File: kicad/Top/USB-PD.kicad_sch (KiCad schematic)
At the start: 37 parts, among them U3 MCP1804 SOT-23-5

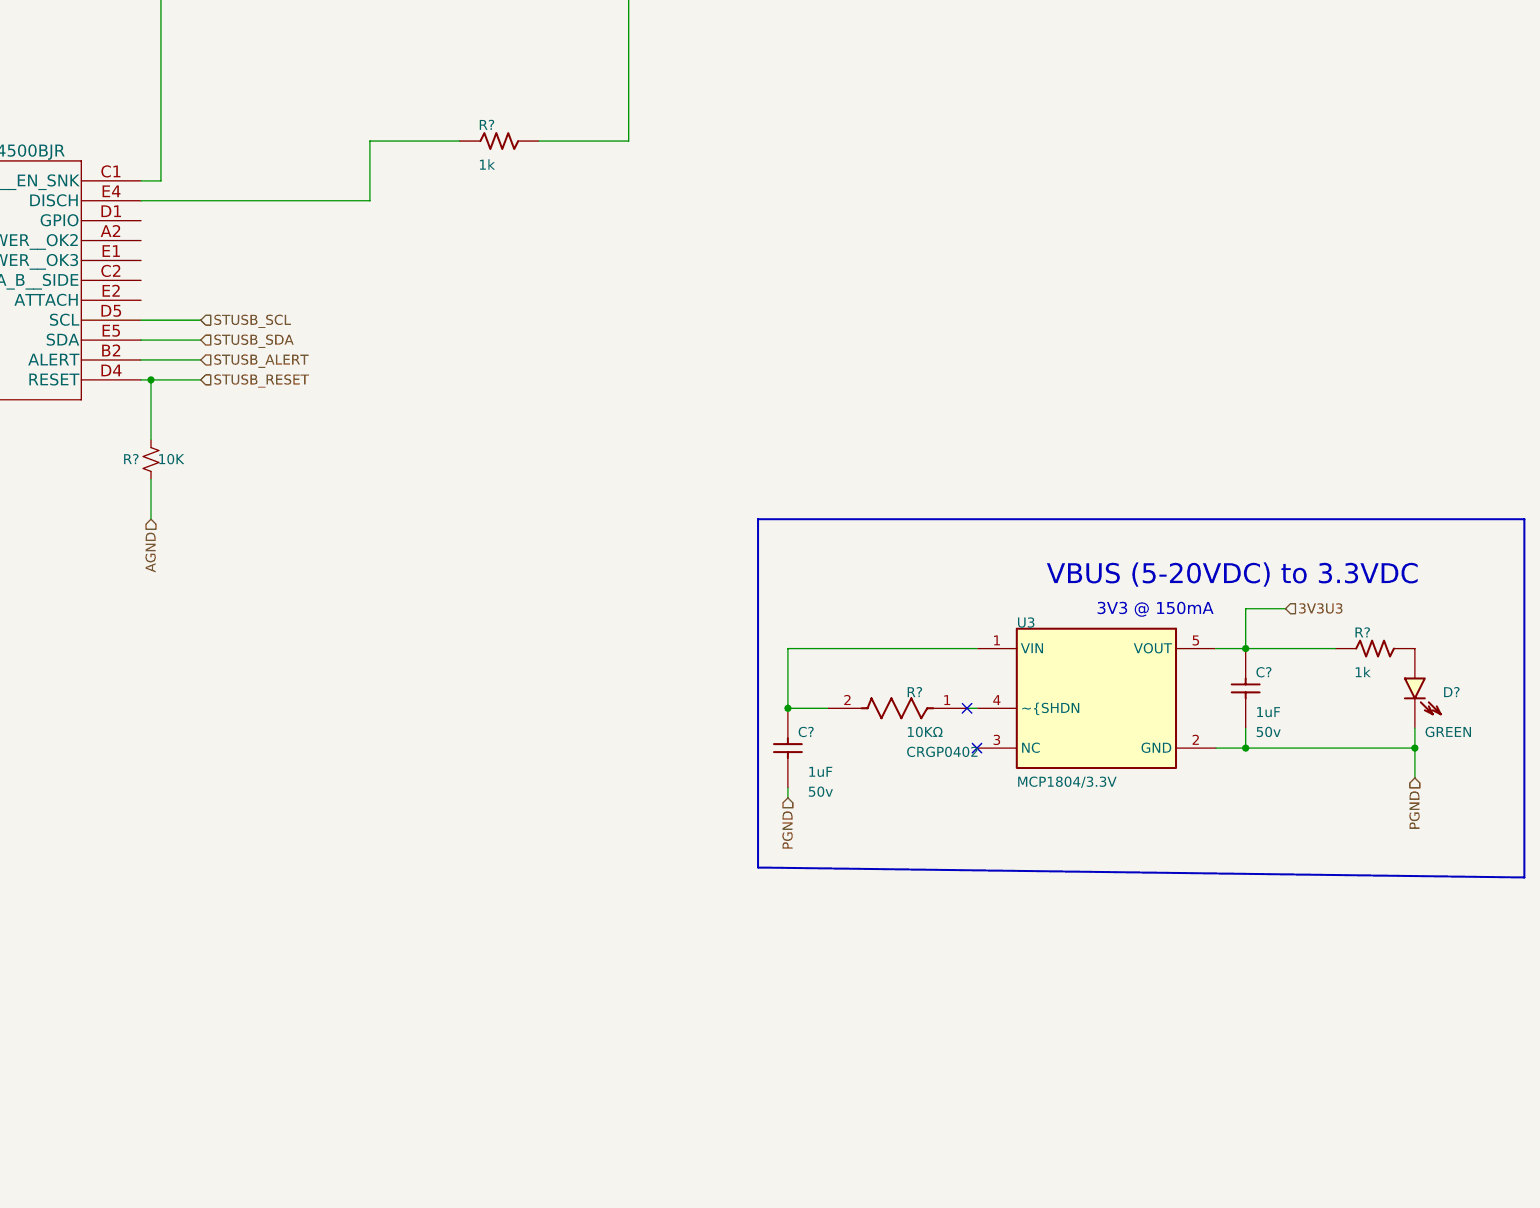
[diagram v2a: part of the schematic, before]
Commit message: Added 3 leds for Pok2,3 and attach
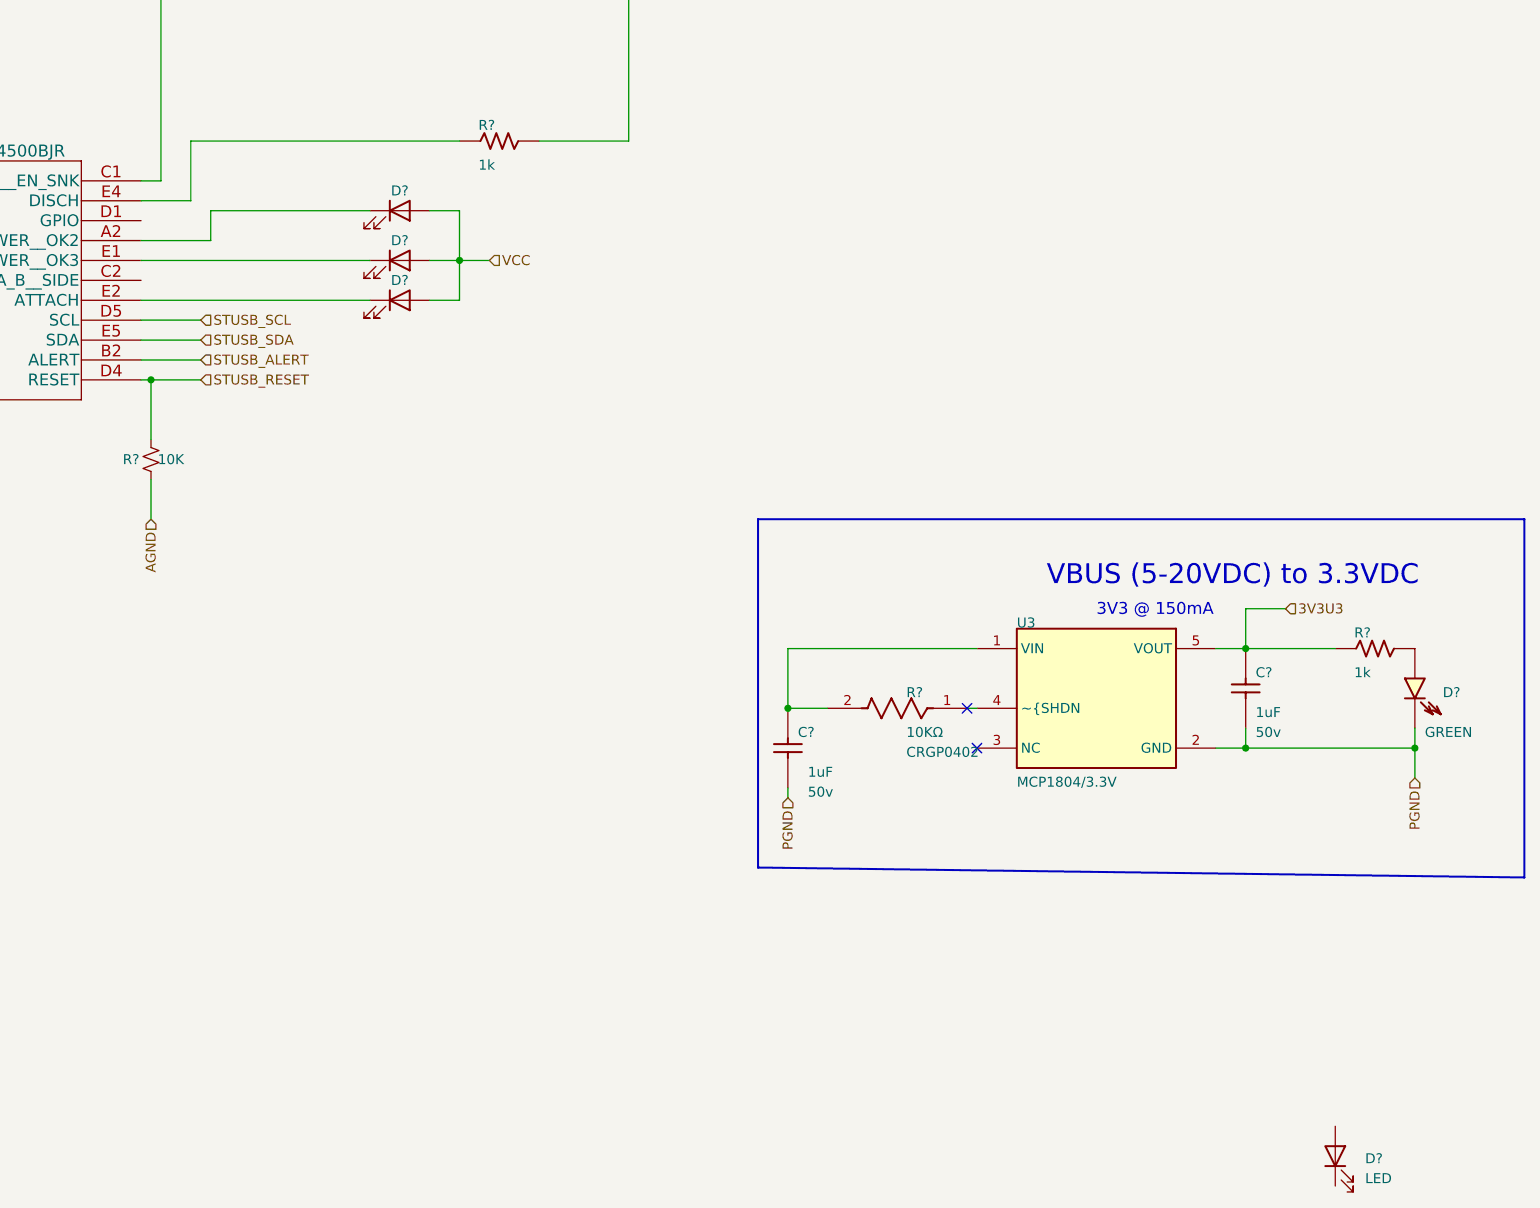
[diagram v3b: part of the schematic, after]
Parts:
- added D? (x4): LED, symbol Device:LED
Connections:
- net VCC: now also D?.2 (A), D?.2 (A), D?.2 (A)
- net at U?.A2 (POWER__OK2): now also D?.1 (K)
- net at U?.E1 (POWER__OK3): now also D?.1 (K)
- net at U?.E2 (ATTACH): now also D?.1 (K)
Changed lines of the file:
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@@
   (junction (at 443.23 454.66) (diameter 0) (color 0 0 0 0)
+  )
+  (junction (at 603.25 411.48) (diameter 0) (color 0 0 0 0)
   )
   (junction (at 444.5 414.02) (diameter 0) (color 0 0 0 0)
@@
     (stroke (width 0) (type default) (color 0 0 0 0))
   )
+  (wire (pts (xy 562.61 403.86) (xy 568.96 403.86))
+    (stroke (width 0) (type default) (color 0 0 0 0))
+  )
   (wire (pts (xy 614.68 300.99) (xy 614.68 306.07))
     (stroke (width 0) (type default) (color 0 0 0 0))
@@
   (wire (pts (xy 417.83 361.95) (xy 416.56 361.95))
     (stroke (width 0.254) (type default) (color 0 0 0 0))
+  )
+  (wire (pts (xy 562.61 416.56) (xy 591.82 416.56))
+    (stroke (width 0) (type default) (color 0 0 0 0))
   )
   (wire (pts (xy 480.06 300.99) (xy 560.07 300.99))
@@
     (stroke (width 0.254) (type default) (color 0 0 0 0))
   )
-  (wire (pts (xy 591.82 403.86) (xy 591.82 396.24))
-    (stroke (width 0) (type default) (color 0 0 0 0))
-  )
   (wire (pts (xy 613.41 396.24) (xy 624.84 396.24))
     (stroke (width 0) (type default) (color 0 0 0 0))
@@
   (wire (pts (xy 577.85 317.5) (xy 598.17 317.5))
     (stroke (width 0.254) (type default) (color 0 0 0 0))
+  )
+  (wire (pts (xy 571.5 408.94) (xy 571.5 405.13))
+    (stroke (width 0) (type default) (color 0 0 0 0))
   )
   (wire (pts (xy 478.79 416.56) (xy 478.79 414.02))
@@
     (stroke (width 0) (type default) (color 0 0 0 0))
   )
+  (wire (pts (xy 562.61 411.48) (xy 591.82 411.48))
+    (stroke (width 0) (type default) (color 0 0 0 0))
+  )
+  (wire (pts (xy 571.5 405.13) (xy 591.82 405.13))
+    (stroke (width 0) (type default) (color 0 0 0 0))
+  )
   (wire (pts (xy 386.08 356.87) (xy 386.08 359.41))
     (stroke (width 0.254) (type default) (color 0 0 0 0))
@@
     (stroke (width 0.254) (type default) (color 0 0 0 0))
   )
+  (wire (pts (xy 603.25 411.48) (xy 607.06 411.48))
+    (stroke (width 0) (type default) (color 0 0 0 0))
+  )
   (wire (pts (xy 521.97 382.27) (xy 521.97 386.08))
     (stroke (width 0) (type default) (color 0 0 0 0))
@@
   )
   (wire (pts (xy 448.31 411.48) (xy 478.79 411.48))
+    (stroke (width 0) (type default) (color 0 0 0 0))
+  )
+  (wire (pts (xy 562.61 408.94) (xy 571.5 408.94))
     (stroke (width 0) (type default) (color 0 0 0 0))
   )
@@
     (stroke (width 0) (type default) (color 0 0 0 0))
   )
+  (wire (pts (xy 603.25 416.56) (xy 603.25 411.48))
+    (stroke (width 0) (type default) (color 0 0 0 0))
+  )
   (wire (pts (xy 598.17 308.61) (xy 598.17 317.5))
     (stroke (width 0.254) (type default) (color 0 0 0 0))
@@
     (stroke (width 0.254) (type default) (color 0 0 0 0))
   )
+  (wire (pts (xy 599.44 411.48) (xy 603.25 411.48))
+    (stroke (width 0) (type default) (color 0 0 0 0))
+  )
   (wire (pts (xy 668.02 468.63) (xy 669.29 468.63))
     (stroke (width 0.254) (type default) (color 0 0 0 0))
@@
   (wire (pts (xy 417.83 359.41) (xy 426.72 359.41))
     (stroke (width 0.254) (type default) (color 0 0 0 0))
+  )
+  (wire (pts (xy 599.44 416.56) (xy 603.25 416.56))
+    (stroke (width 0) (type default) (color 0 0 0 0))
   )
   (wire (pts (xy 645.16 468.63) (xy 645.16 461.01))
@@
     (stroke (width 0.254) (type default) (color 0 0 0 0))
   )
-  (wire (pts (xy 591.82 396.24) (xy 603.25 396.24))
+  (wire (pts (xy 568.96 396.24) (xy 603.25 396.24))
     (stroke (width 0) (type default) (color 0 0 0 0))
   )
@@
   (wire (pts (xy 388.62 364.49) (xy 386.08 364.49))
     (stroke (width 0.254) (type default) (color 0 0 0 0))
+  )
+  (wire (pts (xy 568.96 403.86) (xy 568.96 396.24))
+    (stroke (width 0) (type default) (color 0 0 0 0))
   )
   (wire (pts (xy 603.25 300.99) (xy 614.68 300.99))
@@
     (stroke (width 0.254) (type default) (color 0 0 0 0))
   )
+  (wire (pts (xy 603.25 405.13) (xy 603.25 411.48))
+    (stroke (width 0) (type default) (color 0 0 0 0))
+  )
   (wire (pts (xy 562.61 401.32) (xy 565.15 401.32))
     (stroke (width 0) (type default) (color 0 0 0 0))
@@
     (stroke (width 0.254) (type default) (color 0 0 0 0))
   )
+  (wire (pts (xy 599.44 405.13) (xy 603.25 405.13))
+    (stroke (width 0) (type default) (color 0 0 0 0))
+  )
   (wire (pts (xy 459.74 424.18) (xy 483.87 424.18))
     (stroke (width 0) (type default) (color 0 0 0 0))
@@
   )
   (wire (pts (xy 562.61 419.1) (xy 570.23 419.1))
-    (stroke (width 0) (type default) (color 0 0 0 0))
-  )
-  (wire (pts (xy 562.61 403.86) (xy 591.82 403.86))
     (stroke (width 0) (type default) (color 0 0 0 0))
   )
@@
   )
   (hierarchical_label "STUSB_ALERT" (shape input) (at 570.23 424.18 0)
+    (effects (font (size 1.27 1.27)) (justify left))
+  )
+  (hierarchical_label "VCC" (shape input) (at 607.06 411.48 0)
     (effects (font (size 1.27 1.27)) (justify left))
   )
@@
     (pin "B9")
   )
+  (symbol (lib_id "Device:LED") (at 595.63 416.56 0) (unit 1)
+    (in_bom yes) (on_board yes)
+    (property "Reference" "D?" (id 0) (at 595.63 414.02 0))
+    (property "Value" "LED" (id 1) (at 594.0425 412.75 0)
+      (effects (font (size 1.27 1.27)) hide)
+    )
+    (property "Footprint" "" (id 2) (at 595.63 416.56 0)
+      (effects (font (size 1.27 1.27)) hide)
+    )
+    (property "Datasheet" "~" (id 3) (at 595.63 416.56 0)
+      (effects (font (size 1.27 1.27)) hide)
+    )
+    (pin "1")
+    (pin "2")
+  )
   (symbol (lib_id "Device:C_Small") (at 505.46 379.73 90) (unit 1)
     (in_bom yes) (on_board yes)
@@
     (pin "1")
   )
+  (symbol (lib_id "Device:LED") (at 595.63 411.48 0) (unit 1)
+    (in_bom yes) (on_board yes)
+    (property "Reference" "D?" (id 0) (at 595.63 408.94 0))
+    (property "Value" "LED" (id 1) (at 594.0425 407.67 0)
+      (effects (font (size 1.27 1.27)) hide)
+    )
+    (property "Footprint" "" (id 2) (at 595.63 411.48 0)
+      (effects (font (size 1.27 1.27)) hide)
+    )
+    (property "Datasheet" "~" (id 3) (at 595.63 411.48 0)
+      (effects (font (size 1.27 1.27)) hide)
+    )
+    (pin "1")
+    (pin "2")
+  )
   (symbol (lib_id "ESDA25W:ESDA25W") (at 426.72 416.56 180) (unit 1)
     (in_bom yes) (on_board yes) (fields_autoplaced)
@@
     (pin "3")
   )
+  (symbol (lib_id "Device:LED") (at 595.63 405.13 0) (unit 1)
+    (in_bom yes) (on_board yes)
+    (property "Reference" "D?" (id 0) (at 595.63 402.59 0))
+    (property "Value" "LED" (id 1) (at 591.82 402.59 0)
+      (effects (font (size 1.27 1.27)) hide)
+    )
+    (property "Footprint" "" (id 2) (at 595.63 405.13 0)
+      (effects (font (size 1.27 1.27)) hide)
+    )
+    (property "Datasheet" "~" (id 3) (at 595.63 405.13 0)
+      (effects (font (size 1.27 1.27)) hide)
+    )
+    (pin "1")
+    (pin "2")
+  )
   (symbol (lib_id "Device:R_Small_US") (at 565.15 327.66 180) (unit 1)
     (in_bom yes) (on_board yes)
@@
       (effects (font (size 1.27 1.27)) hide)
     )
+    (pin "1")
+    (pin "2")
+  )
+  (symbol (lib_id "Device:LED") (at 715.01 525.78 90) (unit 1)
+    (in_bom yes) (on_board yes) (fields_autoplaced)
+    (property "Reference" "D?" (id 0) (at 718.82 526.0974 90)
+      (effects (font (size 1.27 1.27)) (justify right))
+    )
+    (property "Value" "LED" (id 1) (at 718.82 528.6374 90)
+      (effects (font (size 1.27 1.27)) (justify right))
+    )
+    (property "Footprint" "" (id 2) (at 715.01 525.78 0)
+      (effects (font (size 1.27 1.27)) hide)
+    )
+    (property "Datasheet" "~" (id 3) (at 715.01 525.78 0)
+      (effects (font (size 1.27 1.27)) hide)
+    )

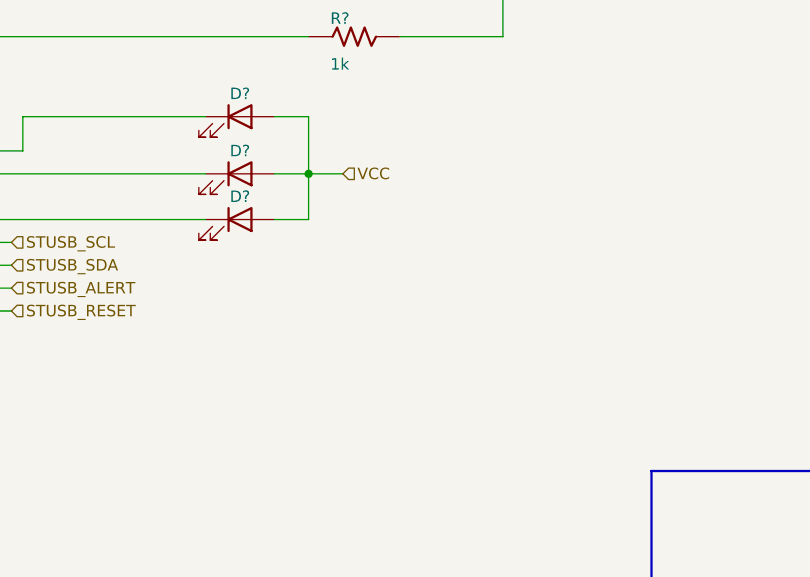
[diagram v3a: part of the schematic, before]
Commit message: Added LED for VCC on
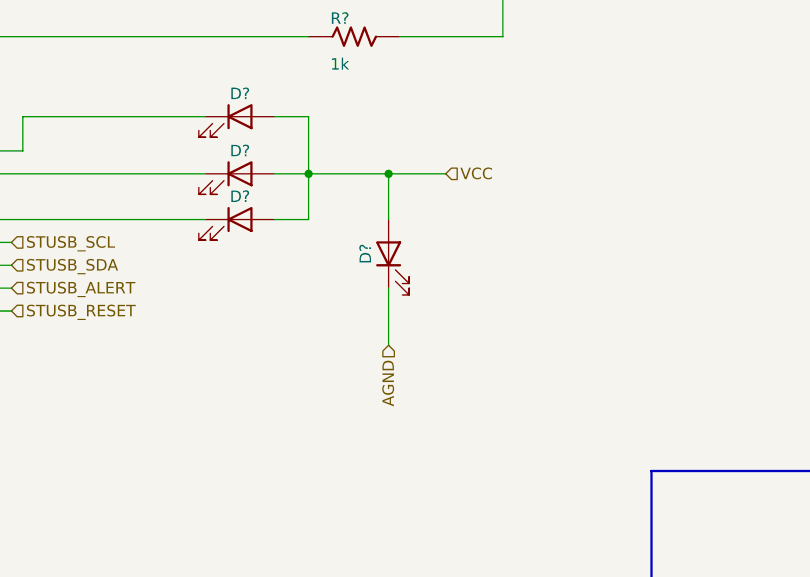
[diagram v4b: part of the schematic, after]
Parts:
- added D?: LED, symbol Device:LED
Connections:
- net AGND: now also D?.1 (K)
- net VCC: now also D?.2 (A)
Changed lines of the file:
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@@
   (junction (at 438.15 300.99) (diameter 0) (color 0 0 0 0)
+  )
+  (junction (at 612.14 411.48) (diameter 0) (color 0 0 0 0)
   )
   (junction (at 386.08 364.49) (diameter 0) (color 0 0 0 0)
@@
     (stroke (width 0.254) (type default) (color 0 0 0 0))
   )
+  (wire (pts (xy 612.14 411.48) (xy 618.49 411.48))
+    (stroke (width 0) (type default) (color 0 0 0 0))
+  )
   (wire (pts (xy 438.15 300.99) (xy 480.06 300.99))
     (stroke (width 0.254) (type default) (color 0 0 0 0))
@@
     (stroke (width 0.254) (type default) (color 0 0 0 0))
   )
-  (wire (pts (xy 603.25 411.48) (xy 607.06 411.48))
+  (wire (pts (xy 603.25 411.48) (xy 612.14 411.48))
     (stroke (width 0) (type default) (color 0 0 0 0))
   )
@@
     (stroke (width 0) (type default) (color 0 0 0 0))
   )
+  (wire (pts (xy 612.14 416.56) (xy 612.14 411.48))
+    (stroke (width 0) (type default) (color 0 0 0 0))
+  )
+  (wire (pts (xy 612.14 424.18) (xy 612.14 430.53))
+    (stroke (width 0) (type default) (color 0 0 0 0))
+  )
   (wire (pts (xy 388.62 359.41) (xy 386.08 359.41))
     (stroke (width 0.254) (type default) (color 0 0 0 0))
@@
     (effects (font (size 1.27 1.27)) (justify left))
   )
-  (hierarchical_label "VCC" (shape input) (at 607.06 411.48 0)
+  (hierarchical_label "VCC" (shape input) (at 618.49 411.48 0)
     (effects (font (size 1.27 1.27)) (justify left))
   )
@@
   (hierarchical_label "VCC" (shape input) (at 436.88 427.99 0)
     (effects (font (size 1.27 1.27)) (justify left))
+  )
+  (hierarchical_label "AGND" (shape input) (at 612.14 430.53 270)
+    (effects (font (size 1.27 1.27)) (justify right))
   )
   (hierarchical_label "STUSB_RESET" (shape input) (at 570.23 426.72 0)
@@
       (effects (font (size 1.27 1.27)) hide)
     )
+    (pin "1")
+    (pin "2")
+  )
+  (symbol (lib_id "Device:LED") (at 612.14 420.37 90) (unit 1)
+    (in_bom yes) (on_board yes)
+    (property "Reference" "D?" (id 0) (at 609.6 420.37 0))
+    (property "Value" "LED" (id 1) (at 608.33 421.9575 0)
+      (effects (font (size 1.27 1.27)) hide)
+    )
+    (property "Footprint" "" (id 2) (at 612.14 420.37 0)
+      (effects (font (size 1.27 1.27)) hide)
+    )
+    (property "Datasheet" "~" (id 3) (at 612.14 420.37 0)
+      (effects (font (size 1.27 1.27)) hide)
+    )

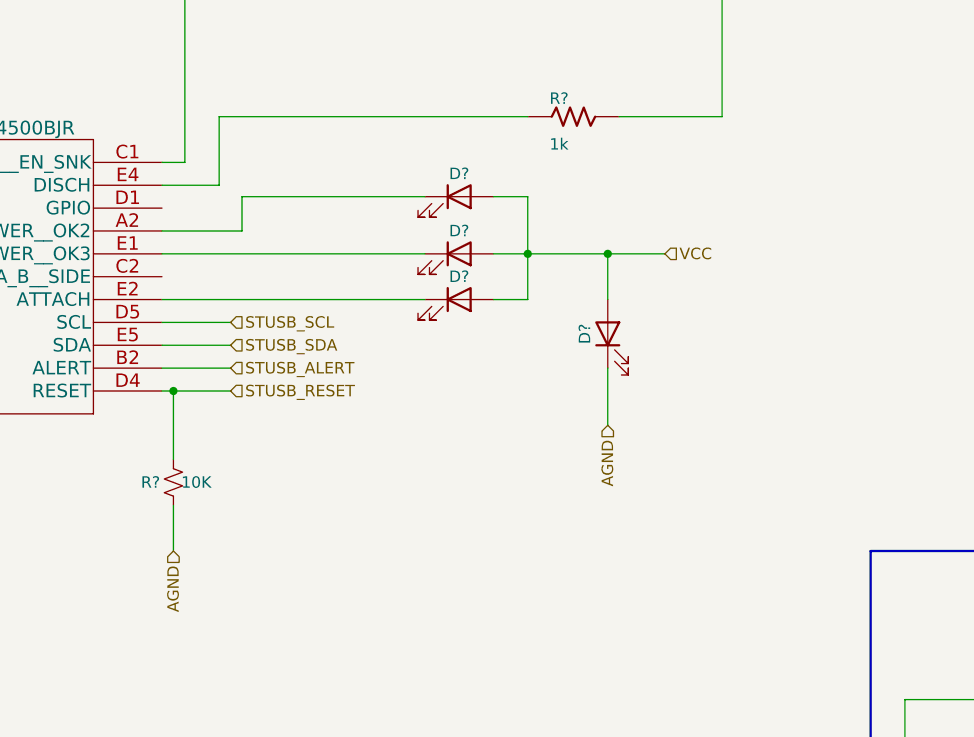
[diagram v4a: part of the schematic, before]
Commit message: Added missing resistors to led paths
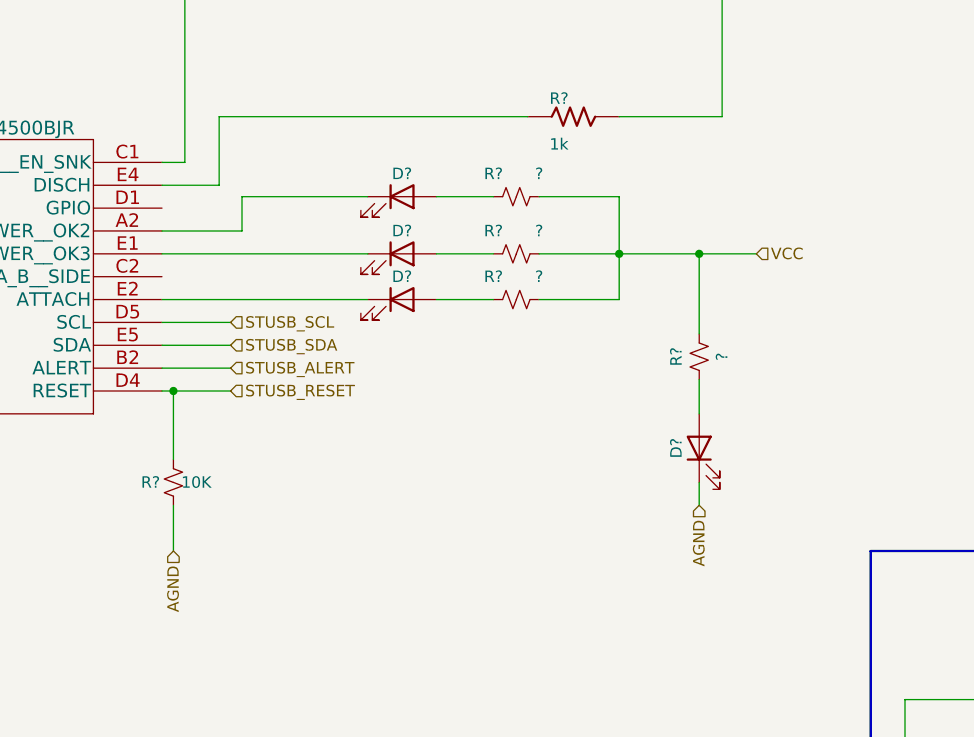
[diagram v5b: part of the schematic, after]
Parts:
- added R? (x4): ?, symbol Device:R_Small_US
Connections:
- net VCC: now also R?.2, R?.2, R?.2, R?.2; no longer D?.2 (A), D?.2 (A), D?.2 (A), D?.2 (A)
- new net: D?.2 (A), R?.1 (x4)
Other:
- moved on the sheet: D?
